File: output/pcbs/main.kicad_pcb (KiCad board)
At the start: 2 copper layers, 228.1 x 75.7 mm, 140 parts

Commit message: Reposition diodes between rows, add MCU battery pins
- Diodes: shift [0, -9.5] places them between switch rows
- MCU: added RAW: BAT_P and GND: GND for battery connection
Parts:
- moved D1 19.0 mm to (50.0, 52.4)
- moved D10 19.0 mm to (107.2, 52.4)
- moved D11 19.0 mm to (107.2, 71.4)
- moved D12 19.0 mm to (107.2, 90.5)
- moved D13 19.0 mm to (126.2, 52.4)
- moved D14 19.0 mm to (126.2, 71.4)
- moved D15 19.0 mm to (126.2, 90.5)
- moved D16 19.0 mm to (145.2, 52.4)
- moved D17 19.0 mm to (145.2, 71.4)
- moved D18 19.0 mm to (145.2, 90.5)
- moved D19 19.0 mm to (164.3, 52.4)
- moved D2 19.0 mm to (50.0, 71.4)
- moved D20 19.0 mm to (164.3, 71.4)
- moved D21 19.0 mm to (164.3, 90.5)
- moved D22 19.0 mm to (183.3, 52.4)
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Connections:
- MCU1 pad 1: RAW -> BAT_P

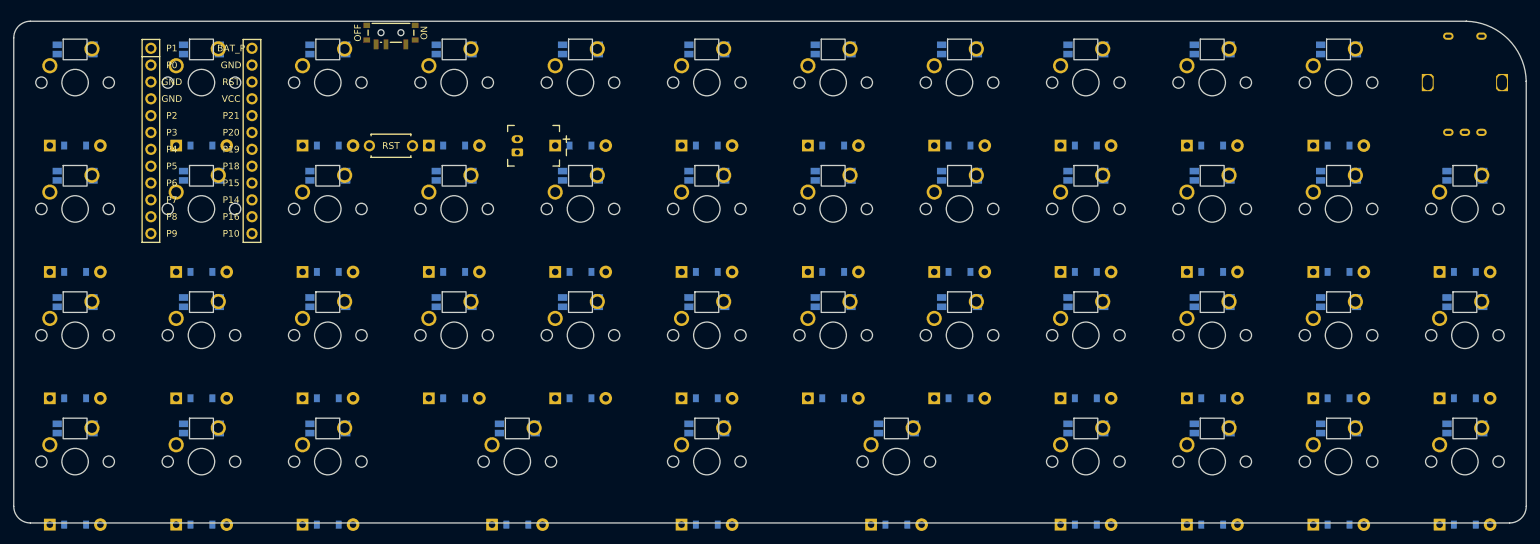
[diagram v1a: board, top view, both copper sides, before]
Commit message: Reposition diodes between rows, add MCU battery pins
- Diodes: shift [0, -9.5] places them between switch rows
- MCU: added RAW: BAT_P and GND: GND for battery connection
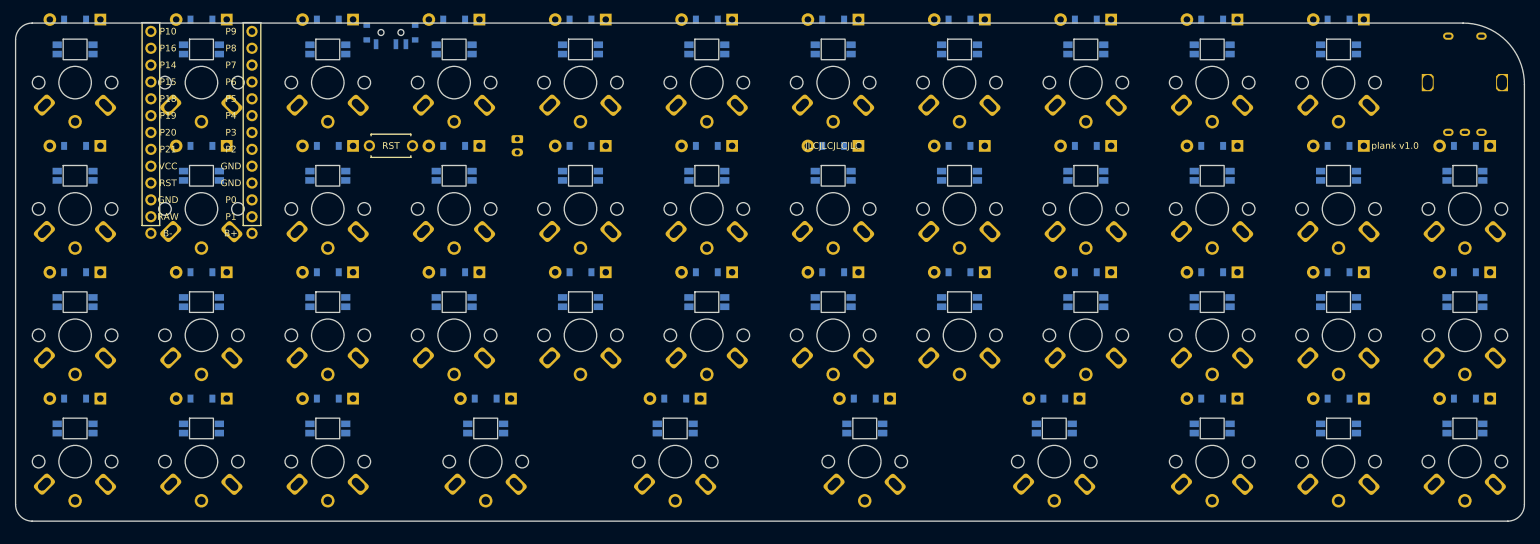
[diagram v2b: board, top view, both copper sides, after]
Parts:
- JST1, PWR1: moved to B.Cu
- MCU1: footprint ceoloide:mcu_supermini_nrf52840 -> MCU_NRF52840
- S1, S10, S11, S12, S13, S14, S15, S16, S17, S18, S19, S2, S20, S21, S22, S23, S24, S25, S26, S27, S28, S29, S3, S30, S31, S32, S33, S34, S35, S36, S37, S38, S39, S4, S40, S41, S42, S43, S44, S45, S5, S6, S7, S8, S9: footprint MX -> Choc+Jerzii
- moved D36 175.6 mm to (221.4, 71.5), turned to 180 degrees
- moved S36 172.5 mm to (221.4, 81.0), turned to 180 degrees
- moved D37 162.7 mm to (221.4, 52.4), turned to 180 degrees
- moved S37 157.1 mm to (221.4, 61.9), turned to 180 degrees
- moved D38 153.6 mm to (221.4, 33.4), turned to 180 degrees
- moved S38 145.1 mm to (221.4, 42.9), turned to 180 degrees
- moved D39 125.3 mm to (240.5, 90.5), turned to 180 degrees
- moved S39 123.8 mm to (240.5, 100.0), turned to 180 degrees
- moved D40 102.6 mm to (240.5, 71.5), turned to 180 degrees
- moved S40 97.1 mm to (240.5, 81.0), turned to 180 degrees
- moved D41 87.8 mm to (240.5, 52.4), turned to 180 degrees
- moved D42 85.1 mm to (240.5, 33.4), turned to 180 degrees
- moved S41 76.8 mm to (240.5, 61.9), turned to 180 degrees
- moved S31 71.4 mm to (197.6, 100.0), turned to 180 degrees
- moved S42 68.7 mm to (240.5, 42.9), turned to 180 degrees
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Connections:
- net LED_45 renamed LED
- D1 pad 1: P1 -> P18
- D1 pad 2: one_top -> one_mod
- D10 pad 1: P20 -> P15
- D10 pad 2: four_top -> three_bottom
- D11 pad 1: P20 -> P21
- D11 pad 2: four_home -> three_home
- D12 pad 1: P20 -> P19
- D12 pad 2: four_bottom -> three_top
- D13 pad 1: P2 -> P18
- D13 pad 2: five_top -> four_mod
- D14 pad 1: P2 -> P15
- D14 pad 2: five_home -> four_bottom
- D15 pad 1: P2 -> P21
- D15 pad 2: five_bottom -> four_home
- D16 pad 1: P3 -> P19
- D16 pad 2: six_top -> four_top
- D17 pad 1: P3 -> P18
- D17 pad 2: six_home -> five_mod
- D18 pad 1: P3 -> P15
- D18 pad 2: six_bottom -> five_bottom
- D19 pad 1: P4 -> P21
- D19 pad 2: seven_top -> five_home
- D2 pad 1: P1 -> P15
- D2 pad 2: one_home -> one_bottom
- D20 pad 1: P4 -> P19
- D20 pad 2: seven_home -> five_top
- D21 pad 1: P4 -> P15
- D21 pad 2: seven_bottom -> six_bottom
- D22 pad 1: P5 -> P21
- D22 pad 2: eight_top -> six_home
- D23 pad 1: P5 -> P19
- D23 pad 2: eight_home -> six_top
- D24 pad 1: P5 -> P15
- D24 pad 2: eight_bottom -> seven_bottom
- D25 pad 1: P6 -> P21
- D25 pad 2: nine_top -> seven_home
- D26 pad 1: P6 -> P19
- D26 pad 2: nine_home -> seven_top
- D27 pad 1: P6 -> P18
- D27 pad 2: nine_bottom -> eight_mod
- D28 pad 1: P7 -> P15
- D28 pad 2: ten_top -> eight_bottom
- D29 pad 1: P7 -> P21
- D29 pad 2: ten_home -> eight_home
- D3 pad 1: P1 -> P21
- D3 pad 2: one_bottom -> one_home
- D30 pad 1: P7 -> P19
- D30 pad 2: ten_bottom -> eight_top
- D31 pad 1: P8 -> P18
- D31 pad 2: eleven_top -> nine_mod
- D32 pad 1: P8 -> P15
- D32 pad 2: eleven_home -> nine_bottom
- D33 pad 1: P8 -> P21
- D33 pad 2: eleven_bottom -> nine_home
- D34 pad 1: P9 -> P19
- D34 pad 2: twelve_home -> nine_top
- D35 pad 1: P9 -> P18
- D35 pad 2: twelve_bottom -> ten_mod
- D36 pad 1: P1 -> P15
- D36 pad 2: one_mod -> ten_bottom
- D37 pad 1: P0 -> P21
- D37 pad 2: two_mod -> ten_home
- D38 pad 1: P14 -> P19
- D38 pad 2: three_mod -> ten_top
- D39 pad 1: P20 -> P18
- D39 pad 2: four_mod -> eleven_mod
- D4 pad 1: P0 -> P19
- D4 pad 2: two_top -> one_top
- D40 pad 1: P2 -> P15
- D40 pad 2: five_mod -> eleven_bottom
- D41 pad 1: P5 -> P21
- D41 pad 2: eight_mod -> eleven_home
- D42 pad 1: P6 -> P19
- D42 pad 2: nine_mod -> eleven_top
- D43 pad 1: P7 -> P18
- D43 pad 2: ten_mod -> twelve_mod
- D44 pad 1: P8 -> P15
- D44 pad 2: eleven_mod -> twelve_bottom
- D45 pad 1: P9 -> P21
- D45 pad 2: twelve_mod -> twelve_home
- D5 pad 1: P0 -> P18
- D5 pad 2: two_home -> two_mod
- D6 pad 1: P0 -> P15
- D7 pad 1: P14 -> P21
- D7 pad 2: three_top -> two_home
- D8 pad 1: P14 -> P19
- D8 pad 2: three_home -> two_top
- D9 pad 1: P14 -> P18
- D9 pad 2: three_bottom -> three_mod
- LED1 pad 2: LED_1 -> LED_4
- LED1 pad 4: LED_DIN -> LED_3
- LED10 pad 2: LED_10 -> LED_11
- LED10 pad 4: LED_9 -> LED_10
- LED11 pad 2: LED_11 -> LED_10
- LED11 pad 4: LED_10 -> LED_9
- LED12 pad 2: LED_12 -> LED_9
- LED12 pad 4: LED_11 -> LED_8
- LED17 pad 2: LED_17 -> LED_20
- LED17 pad 4: LED_16 -> LED_19
- LED18 pad 2: LED_18 -> LED_19
- LED18 pad 4: LED_17 -> LED_18
- LED19 pad 2: LED_19 -> LED_18
- LED19 pad 4: LED_18 -> LED_17
- LED2 pad 2: LED_2 -> LED_3
- LED2 pad 4: LED_1 -> LED_2
- LED20 pad 2: LED_20 -> LED_17
- LED20 pad 4: LED_19 -> LED_16
- LED24 pad 2: LED_24 -> LED_26
- LED24 pad 4: LED_23 -> LED_25
- LED26 pad 2: LED_26 -> LED_24
- LED26 pad 4: LED_25 -> LED_23
- LED3 pad 2: LED_3 -> LED_2
- LED3 pad 4: LED_2 -> LED_1
- LED31 pad 2: LED_31 -> LED_34
- LED31 pad 4: LED_30 -> LED_33
- LED32 pad 2: LED_32 -> LED_33
- LED32 pad 4: LED_31 -> LED_32
- LED33 pad 2: LED_33 -> LED_32
- LED33 pad 4: LED_32 -> LED_31
- LED34 pad 2: LED_34 -> LED_31
- LED34 pad 4: LED_33 -> LED_30
- LED39 pad 2: LED_39 -> LED_42
- LED39 pad 4: LED_38 -> LED_41
- LED4 pad 2: LED_4 -> LED_1
- LED4 pad 4: LED_3 -> LED_DIN
- LED40 pad 2: LED_40 -> LED_41
- LED40 pad 4: LED_39 -> LED_40
- LED41 pad 2: LED_41 -> LED_40
- LED41 pad 4: LED_40 -> LED_39
- LED42 pad 2: LED_42 -> LED_39
- LED42 pad 4: LED_41 -> LED_38
- LED9 pad 2: LED_9 -> LED_12
- LED9 pad 4: LED_8 -> LED_11
- MCU1 pad 1: BAT_P -> P1
- MCU1 pad 10: P14 -> P7
- MCU1 pad 11: P16 -> P8
- MCU1 pad 12: P10 -> P9
- MCU1 pad 13: P9 -> P10
- MCU1 pad 14: P8 -> P16
- MCU1 pad 15: P7 -> P14
- MCU1 pad 16: P6 -> P15
- MCU1 pad 17: P5 -> P18
- MCU1 pad 18: P4 -> P19
- MCU1 pad 19: P3 -> P20
- MCU1 pad 2: GND -> P0
- MCU1 pad 20: P2 -> P21
- MCU1 pad 21: GND -> VCC
- MCU1 pad 22: GND -> RST
- MCU1 pad 23: P0 -> GND
- MCU1 pad 24: P1 -> RAW
- MCU1 pad 3: RST -> GND
- MCU1 pad 4: VCC -> GND
- MCU1 pad 5: P21 -> P2
- MCU1 pad 6: P20 -> P3
- MCU1 pad 7: P19 -> P4
- MCU1 pad 8: P18 -> P5
- MCU1 pad 9: P15 -> P6
- PWR1 pad 1: BAT_P -> (no net)
- PWR1 pad 2: RAW -> BAT_P
- PWR1 pad 3: (no net) -> RAW
- RE1 pad S2: GND -> (no net)
- RST1 pad 1: RST -> GND
- RST1 pad 2: GND -> RST
- S1 pad 2: one_top -> one_mod
- S10 pad 1: P20 -> P14
- S10 pad 2: four_top -> three_bottom
- S11 pad 1: P20 -> P14
- S11 pad 2: four_home -> three_home
- S12 pad 1: P20 -> P14
- S12 pad 2: four_bottom -> three_top
- S13 pad 1: P2 -> P20
- S13 pad 2: five_top -> four_mod
- S14 pad 1: P2 -> P20
- S14 pad 2: five_home -> four_bottom
- S15 pad 1: P2 -> P20
- S15 pad 2: five_bottom -> four_home
- S16 pad 1: P3 -> P20
- S16 pad 2: six_top -> four_top
- S17 pad 1: P3 -> P2
- S17 pad 2: six_home -> five_mod
- S18 pad 1: P3 -> P2
- S18 pad 2: six_bottom -> five_bottom
- S19 pad 1: P4 -> P2
- S19 pad 2: seven_top -> five_home
- S2 pad 2: one_home -> one_bottom
- S20 pad 1: P4 -> P2
- S20 pad 2: seven_home -> five_top
- S21 pad 1: P4 -> P3
- S21 pad 2: seven_bottom -> six_bottom
- S22 pad 1: P5 -> P3
- S22 pad 2: eight_top -> six_home
- S23 pad 1: P5 -> P3
- S23 pad 2: eight_home -> six_top
- S24 pad 1: P5 -> P4
- S24 pad 2: eight_bottom -> seven_bottom
- S25 pad 1: P6 -> P4
- S25 pad 2: nine_top -> seven_home
- S26 pad 1: P6 -> P4
- S26 pad 2: nine_home -> seven_top
- S27 pad 1: P6 -> P5
- S27 pad 2: nine_bottom -> eight_mod
- S28 pad 1: P7 -> P5
- S28 pad 2: ten_top -> eight_bottom
- S29 pad 1: P7 -> P5
- S29 pad 2: ten_home -> eight_home
- S3 pad 2: one_bottom -> one_home
- S30 pad 1: P7 -> P5
- S30 pad 2: ten_bottom -> eight_top
- S31 pad 1: P8 -> P6
- S31 pad 2: eleven_top -> nine_mod
- S32 pad 1: P8 -> P6
- S32 pad 2: eleven_home -> nine_bottom
- S33 pad 1: P8 -> P6
- S33 pad 2: eleven_bottom -> nine_home
- S34 pad 1: P9 -> P6
- S34 pad 2: twelve_home -> nine_top
- S35 pad 1: P9 -> P7
- S35 pad 2: twelve_bottom -> ten_mod
- S36 pad 1: P1 -> P7
- S36 pad 2: one_mod -> ten_bottom
- S37 pad 1: P0 -> P7
- S37 pad 2: two_mod -> ten_home
- S38 pad 1: P14 -> P7
- S38 pad 2: three_mod -> ten_top
- S39 pad 1: P20 -> P8
- S39 pad 2: four_mod -> eleven_mod
- S4 pad 1: P0 -> P1
- S4 pad 2: two_top -> one_top
- S40 pad 1: P2 -> P8
- S40 pad 2: five_mod -> eleven_bottom
- S41 pad 1: P5 -> P8
- S41 pad 2: eight_mod -> eleven_home
- S42 pad 1: P6 -> P8
- S42 pad 2: nine_mod -> eleven_top
- S43 pad 1: P7 -> P9
- S43 pad 2: ten_mod -> twelve_mod
- S44 pad 1: P8 -> P9
- S44 pad 2: eleven_mod -> twelve_bottom
- S45 pad 2: twelve_mod -> twelve_home
- S5 pad 2: two_home -> two_mod
- S7 pad 1: P14 -> P0
- S7 pad 2: three_top -> two_home
- S8 pad 1: P14 -> P0
- S8 pad 2: three_home -> two_top
- S9 pad 2: three_bottom -> three_mod
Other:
- board size 228.1 x 75.7 mm -> 227.5 x 75.1 mm
- board text added: "JLCJLCJLCJLC"
- board text added: "plank v1.0"
